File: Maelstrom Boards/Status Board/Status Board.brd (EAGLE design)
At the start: 101.6 x 101.6 mm, 14 parts, among them P1 39-30-04?

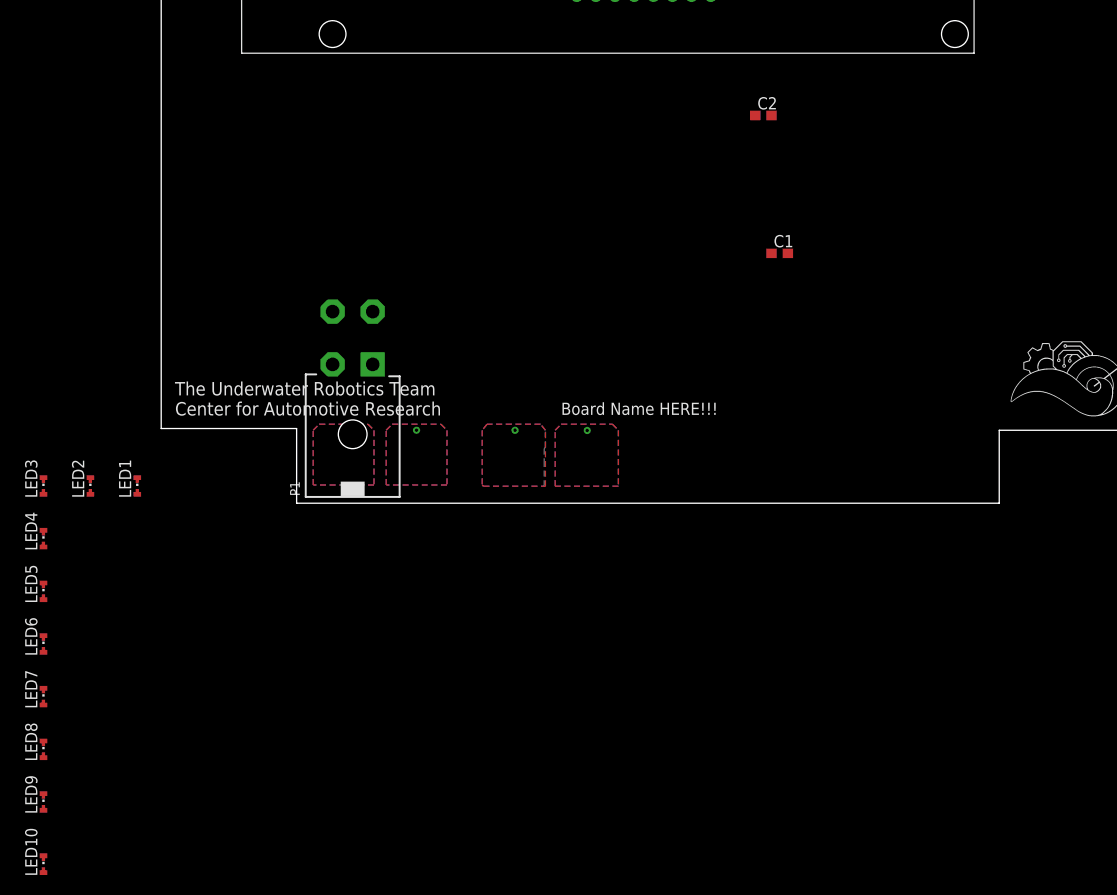
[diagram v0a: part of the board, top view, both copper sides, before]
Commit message: Adding LEDs
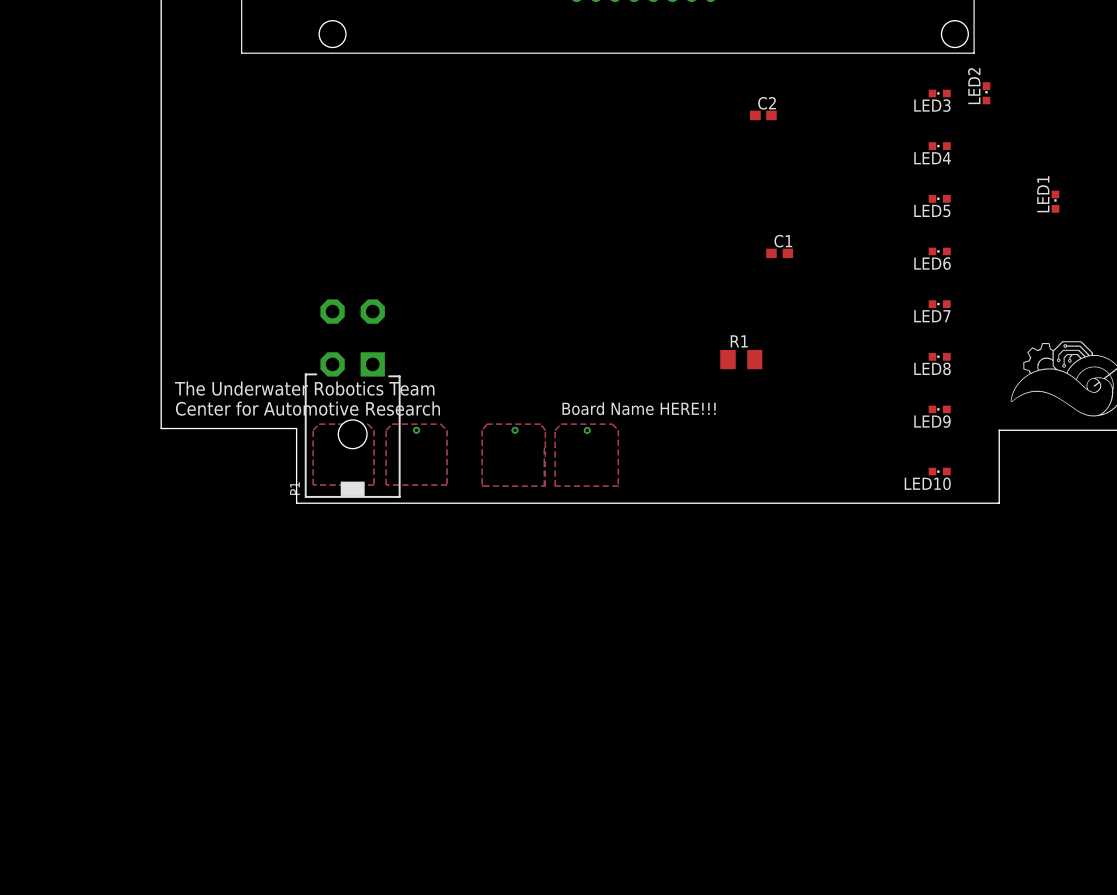
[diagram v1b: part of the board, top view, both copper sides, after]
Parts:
- added R1: (no value), rcl:M3216
- LED1, LED10, LED2, LED3, LED4, LED5, LED6, LED7, LED8, LED9: device led:CHIPLED-0603-TTW -> led:CHIPLED_0603
- moved LED10 102.2 mm to (81.3, 3.30), turned to 90 degrees
- moved LED2 102.2 mm to (86.2, 42.8)
- moved LED3 102.2 mm to (81.3, 42.8), turned to 90 degrees
- moved LED4 102.2 mm to (81.3, 37.3), turned to 90 degrees
- moved LED5 102.2 mm to (81.3, 31.8), turned to 90 degrees
- moved LED6 102.2 mm to (81.3, 26.3), turned to 90 degrees
- moved LED7 102.2 mm to (81.3, 20.8), turned to 90 degrees
- moved LED8 102.2 mm to (81.3, 15.3), turned to 90 degrees
- moved LED9 102.2 mm to (81.3, 9.80), turned to 90 degrees
- moved LED1 100.4 mm to (93.4, 31.5)
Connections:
- new net N$4: LED1.A, LED10.A, LED2.A, LED3.A, LED4.A, LED5.A, LED6.A, LED7.A, LED8.A, LED9.A, R1.1
- net +3V3: now also R1.2
- net GND: now also LED1.C, LED10.C, LED2.C, LED3.C, LED4.C, LED5.C, LED6.C, LED7.C, LED8.C, LED9.C

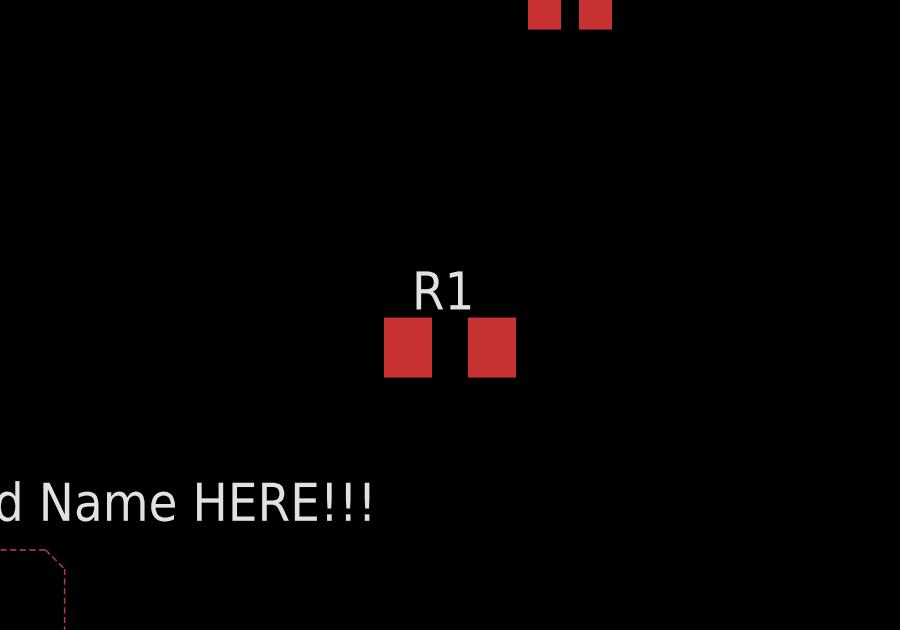
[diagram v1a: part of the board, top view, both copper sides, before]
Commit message: Removing Resistor
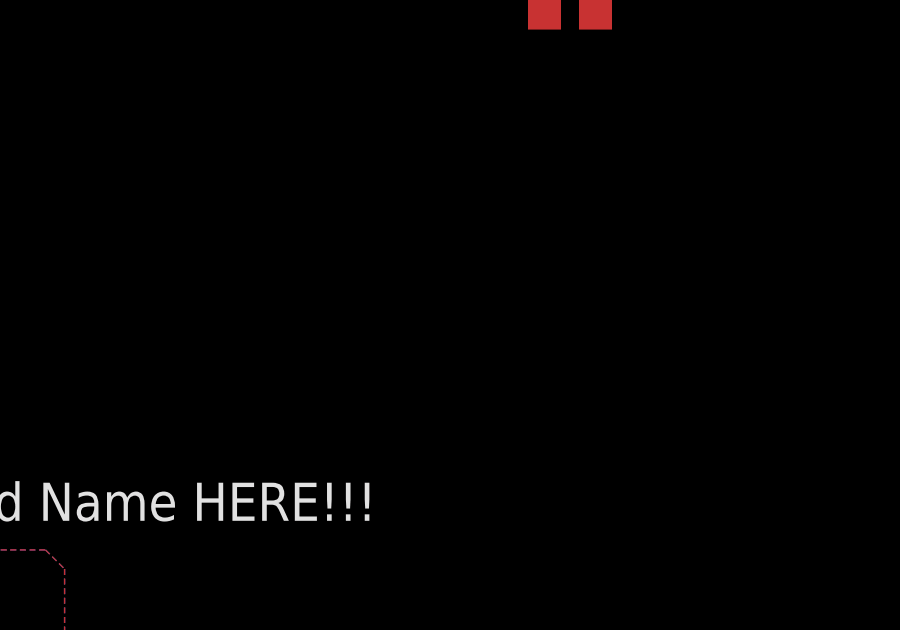
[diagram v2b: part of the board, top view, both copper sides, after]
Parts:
- removed R1: (no value), rcl:M3216
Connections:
- net +3V3: no longer R1.2
- net N$4: no longer R1.1
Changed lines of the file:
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@@
 <attribute name="VALUE" x="82.57" y="5.205" size="1.27" layer="27" rot="R180"/>
-</element>
-<element name="R1" library="rcl" library_urn="urn:adsk.eagle:library:334" package="M3216" package3d_urn="urn:adsk.eagle:package:23563/1" value="" x="60.6" y="15" smashed="yes">
-<attribute name="NAME" x="59.33" y="16.27" size="1.27" layer="25"/>
-<attribute name="SPICEPREFIX" value="R" x="60.6" y="15" size="1.778" layer="27" display="off"/>
-<attribute name="VALUE" x="59.33" y="12.46" size="1.27" layer="27"/>
 </element>
 </elements>
@@
 <contactref element="U$1" pad="VDD"/>
 <contactref element="U$1" pad="RST"/>
-<contactref element="R1" pad="2"/>
 <wire x1="43.4" y1="53" x2="51.4" y2="53" width="0" layer="19" extent="1-1"/>
 <wire x1="17.9045" y1="14.5" x2="43.4" y2="53" width="0" layer="19" extent="1-1"/>
 <wire x1="19" y1="7.6" x2="17.9045" y2="14.5" width="0" layer="19" extent="1-1"/>
-<wire x1="62" y1="15" x2="19" y2="7.6" width="0" layer="19" extent="1-1"/>
 </signal>
 <signal name="SDA">
@@
 <contactref element="LED8" pad="A"/>
 <contactref element="LED9" pad="A"/>
-<contactref element="R1" pad="1"/>
 <wire x1="82.05" y1="42.8" x2="86.2" y2="42.05" width="0" layer="19" extent="1-1"/>
 <wire x1="82.05" y1="37.3" x2="82.05" y2="42.8" width="0" layer="19" extent="1-1"/>
@@
 <wire x1="82.05" y1="3.3" x2="82.05" y2="9.8" width="0" layer="19" extent="1-1"/>
 <wire x1="93.4" y1="30.75" x2="82.05" y2="31.8" width="0" layer="19" extent="1-1"/>
-<wire x1="59.2" y1="15" x2="82.05" y2="3.3" width="0" layer="19" extent="1-1"/>
 </signal>
 </signals>

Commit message: Update Status Board
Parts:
- added R1: 23.333333, rcl:M3216
- moved LED4 89.0 mm to (6.50, 85.6)
- moved LED5 85.2 mm to (6.00, 71.6)
- moved LED6 77.0 mm to (6.70, 45.5)
- moved LED10 67.8 mm to (88.6, 70.7)
- moved LED7 65.3 mm to (19.2, 41.1)
- moved LED3 64.3 mm to (33.9, 86.2), turned to 0 degrees
- moved LED1 53.9 mm to (88.0, 85.1)
- moved LED2 52.3 mm to (57.4, 86.4)
- moved LED8 46.3 mm to (43.3, 41.7)
- moved LED9 35.6 mm to (88.0, 44.8)
- moved C1 21.9 mm to (50.8, 43.1), turned to 180 degrees
- moved C2 7.38 mm to (57.3, 45.3)
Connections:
- net +3V3: now also R1.2
- net N$4: now also R1.1
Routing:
- net GND: track 0.00 -> 268.5 mm, vias 2 -> 6
- net N$4: track 0.00 -> 238.2 mm, vias 0 -> 2
- net +3V3: track 0.00 -> 94.3 mm, vias 1 -> 3
- net SDA: track 0.00 -> 48.6 mm
- net SCL: track 0.00 -> 42.6 mm
- net N$3: track 0.00 -> 10.6 mm
- net N$2: track 0.00 -> 8.01 mm
- net N$1: track 0.00 -> 7.97 mm

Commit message: Finished status board schematic
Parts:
- added C3: 1uF, rcl:C0603
- added C4: 0.1uF, rcl:C0603
- added IC1: LM555D, linear:SO08
- added Q1: 310mA/60V/1.6Ω, SparkFun-DiscreteSemi:SOT323
- added R2: 70, rcl:R0603
- added R3, R4: 15, rcl:R0603
- added R5: 50k, rcl:R0603
- added R6: 100k, rcl:R0603
- added R7: 10k, rcl:R0603
- added RG, RV+: 0, rcl:R0603
- added U$2: MAX7315, MAX7315:TSSOP-16
- C1, C2: value (none) -> 1uF
- R1: value 23.333333 -> 6.8; device rcl:M3216 -> rcl:R0603
- moved R1 97.2 mm to (-14.7, -46.5)
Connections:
- new net BLINK: IC1.3, Q1.1
- new net BLINK_OFF: IC1.4, R7.2, U$2.7
- new net BLUE: R4.2, U$2.6
- new net GREEN: R3.2, U$2.5
- new net N$10: C3.1, IC1.2, IC1.6, R5.2, R6.1
- new net N$20: LED1.C, LED10.C, LED2.C, LED3.C, LED4.C, LED5.C, LED6.C, LED7.C, LED8.C, LED9.C, Q1.3
- new net N$4: C2.2, U$1.C1+
- new net N$5: R3.1, U$1.GK
- new net N$6: RG.2, RV+.1, U$2.1, U$2.2, U$2.3
- new net N$7: R2.1, U$1.RK
- new net N$9: IC1.7, R5.1
- new net RED: R2.2, U$2.4
- net +3V3: now also C4.1, IC1.8, R6.2, R7.1, RV+.2, U$1.A, U$2.16
- net GND: now also C3.2, C4.2, IC1.1, Q1.2, RG.1, U$2.8; no longer LED1.C, LED10.C, LED2.C, LED3.C, LED4.C, LED5.C, LED6.C, LED7.C, LED8.C, LED9.C
- net N$1: now also R4.1, U$1.BK; no longer C2.1, U$1.C1+
- net N$2: now also C2.1; no longer C2.2
- net SCL: now also U$2.14
- net SDA: now also U$2.15
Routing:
- net GND: track 268.5 -> 6.78 mm, vias 6 -> 0
- net N$20: track 0.00 -> 250.4 mm, vias 0 -> 6
- net N$11: track 238.2 -> 141.3 mm
- net +3V3: track 94.3 -> 52.0 mm, vias 3 -> 1
- net N$2: track 8.01 -> 0.00 mm
- net N$4: track 0.00 -> 7.97 mm
- net N$1: track 7.97 -> 0.00 mm
- net N$3: track 10.6 -> 8.15 mm

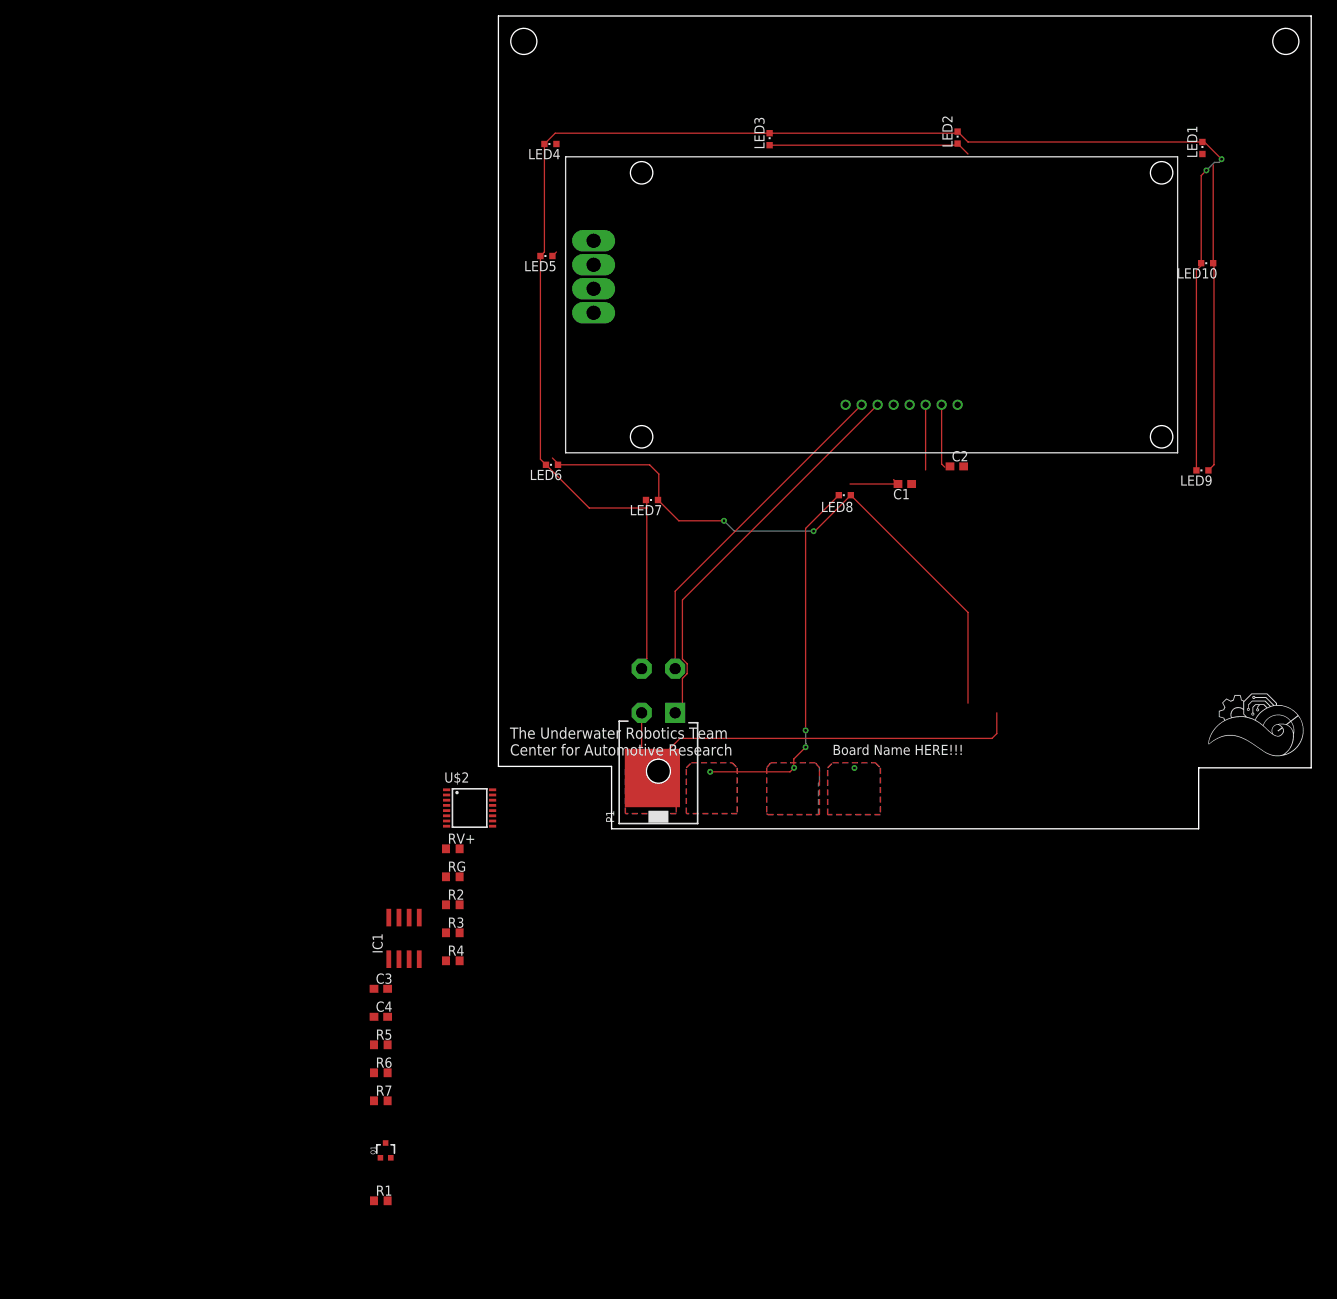
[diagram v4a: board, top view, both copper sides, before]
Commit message: Setting board dimensions and adding back ground plane
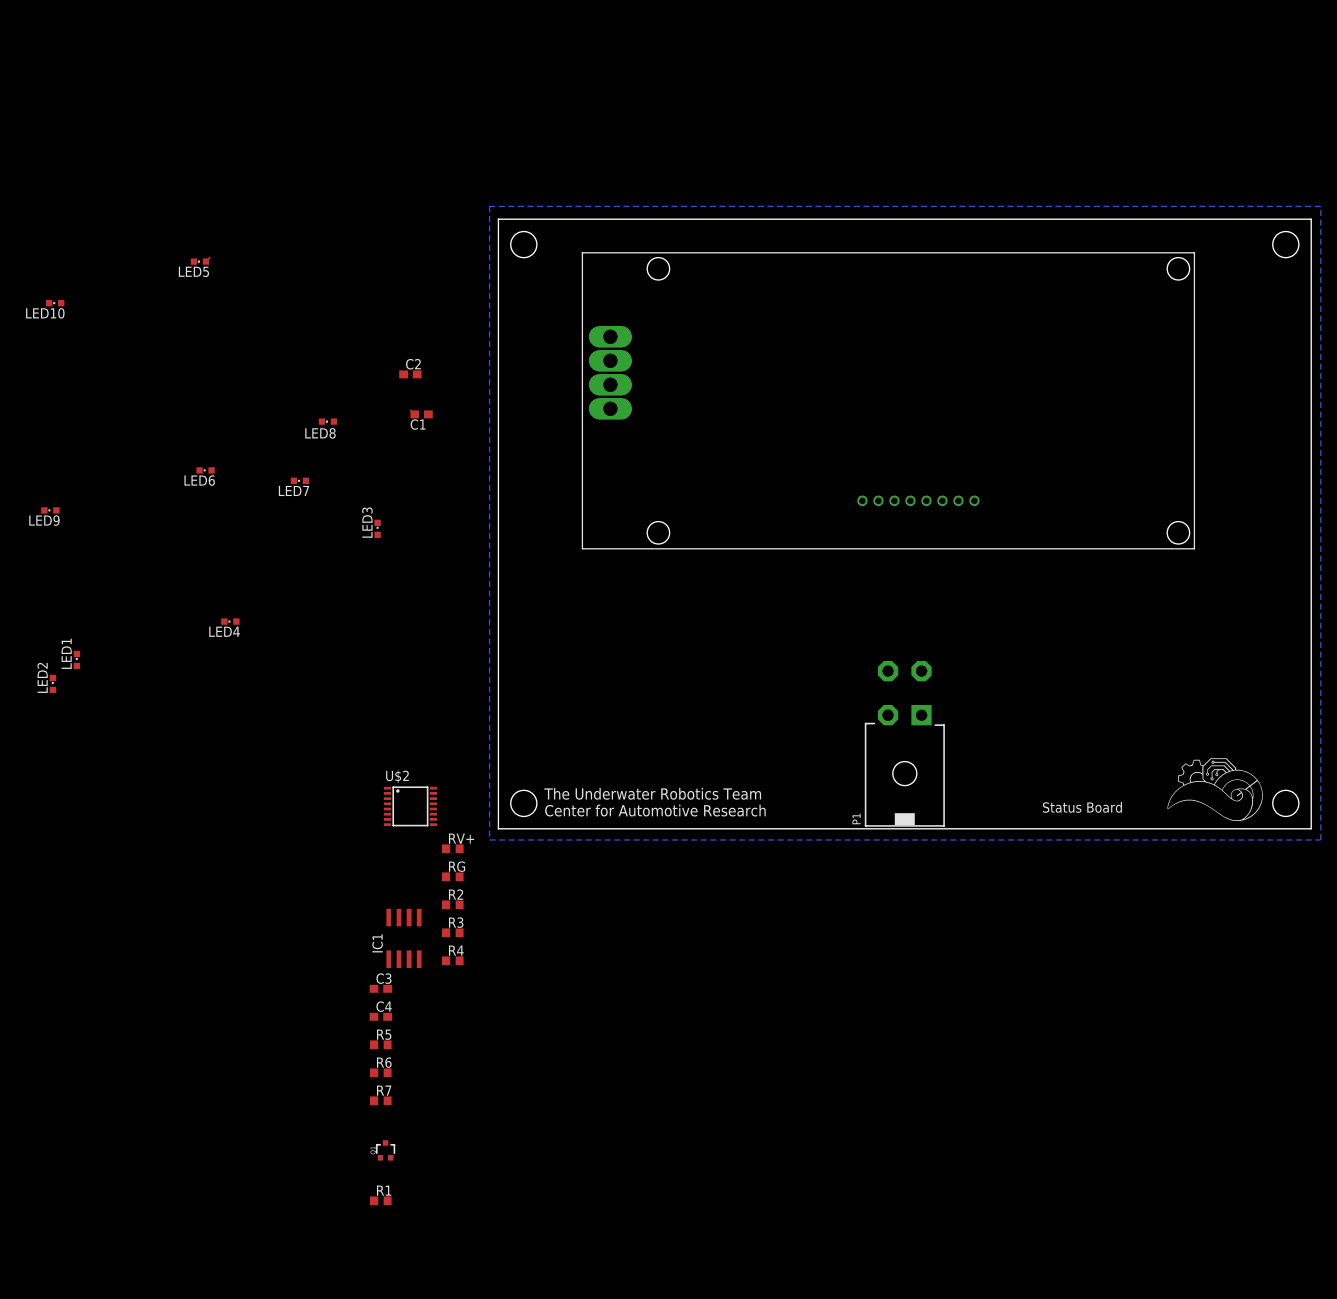
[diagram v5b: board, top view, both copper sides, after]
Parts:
- moved LED1 154.6 mm to (-52.7, 21.1)
- moved LED10 144.1 mm to (-55.4, 65.7)
- moved LED9 144.1 mm to (-56.0, 39.8)
- moved LED2 132.1 mm to (-55.7, 18.1)
- moved LED4 71.9 mm to (-33.5, 25.9)
- moved C2 69.3 mm to (-11.0, 56.8)
- moved LED3 69.1 mm to (-15.1, 37.5)
- moved LED8 65.3 mm to (-21.3, 50.9)
- moved C1 61.0 mm to (-9.60, 51.8)
- moved LED7 44.1 mm to (-24.8, 43.5)
- moved LED6 43.3 mm to (-36.6, 44.8)
- moved LED5 43.3 mm to (-37.3, 70.9)
- moved P1 30.8 mm to (50.8, 14.2)
- moved U$1 12.2 mm to (20.0, 37.0)
- moved U$2 7.40 mm to (-11.0, 2.80)
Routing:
- net N$20: track 250.4 -> 0.53 mm, vias 6 -> 0
- net N$11: track 141.3 -> 0.71 mm, vias 2 -> 0
- net +3V3: track 52.0 -> 0.00 mm, vias 1 -> 0
- net SDA: track 48.6 -> 0.00 mm
- net SCL: track 42.6 -> 0.14 mm
- net N$3: track 8.15 -> 0.00 mm
- net N$4: track 7.97 -> 0.00 mm
- net GND: track 6.78 -> 0.78 mm
- removed copper zone on layer 1, net +3V3
- removed copper zone on layer 16, net +3V3
- removed copper zone on layer 1, net +5V
- removed copper zone on layer 16, net +5V
- removed copper zone on layer 1, net GND
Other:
- board size 101.6 x 101.6 mm -> 101.6 x 76.2 mm
- board text added: "Status Board"
- board text removed: "Board Name HERE!!!"
